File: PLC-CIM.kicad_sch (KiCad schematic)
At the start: 1 part, among them U1 ESP32-DEVKITC

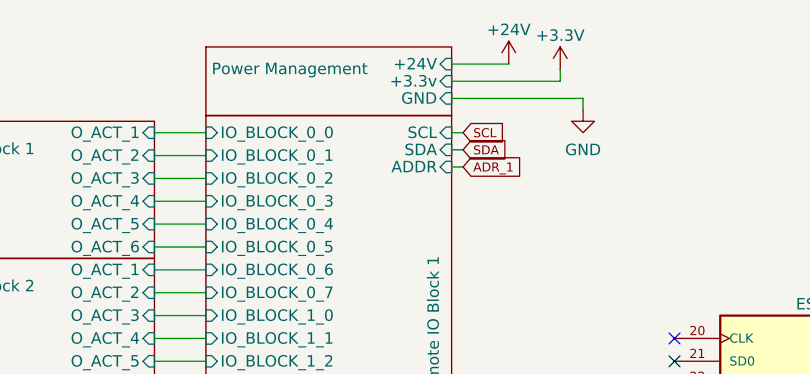
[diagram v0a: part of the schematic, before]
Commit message: Automate library addition * Added script to automagically extract samacsys libraries and put them in corresponding folders. * Note: Requires zsh
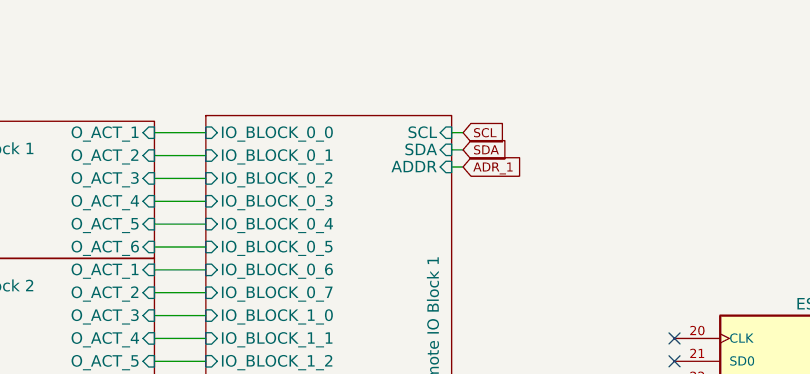
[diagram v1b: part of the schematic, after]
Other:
- removed sheet Power Management
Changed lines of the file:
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@@
-    (stroke (width 0) (type default))
-  )
-  (wire (pts (xy 120.65 63.5) (xy 132.715 63.5))
     (stroke (width 0) (type default))
   )
@@
     (stroke (width 0) (type default))
   )
-  (wire (pts (xy 135.255 65.405) (xy 120.65 65.405))
-    (stroke (width 0) (type default))
-  )
   (wire (pts (xy 120.65 171.45) (xy 122.555 171.45))
     (stroke (width 0) (type default))
@@
     (stroke (width 0) (type default))
   )
-  (wire (pts (xy 135.255 66.675) (xy 135.255 65.405))
-    (stroke (width 0) (type default))
-  )
   (wire (pts (xy 136.525 123.825) (xy 136.525 122.555))
     (stroke (width 0) (type default))
@@
     (stroke (width 0) (type default))
   )
-  (wire (pts (xy 120.65 61.595) (xy 127 61.595))
-    (stroke (width 0) (type default))
-  )
   (wire (pts (xy 90.17 128.905) (xy 93.345 128.905))
     (stroke (width 0) (type default))
@@
     (stroke (width 0) (type default))
   )
-  (wire (pts (xy 132.715 63.5) (xy 132.715 62.23))
-    (stroke (width 0) (type default))
-  )
   (wire (pts (xy 120.65 180.975) (xy 122.555 180.975))
     (stroke (width 0) (type default))
@@
     )
   )
-  (symbol (lib_id "power:GND") (at 135.255 66.675 0) (unit 1)
+  (symbol (lib_id "power:+3.3V") (at 198.12 137.795 0) (unit 1)
     (in_bom yes) (on_board yes) (dnp no) (fields_autoplaced)
-    (property "Reference" "#PWR088" (at 135.255 73.025 0)
-      (effects (font (size 1.27 1.27)) hide)
-    )
-    (property "Value" "GND" (at 135.255 71.12 0)
+    (property "Reference" "#PWR0102" (at 198.12 141.605 0)
+      (effects (font (size 1.27 1.27)) hide)
+    )
+    (property "Value" "+3.3V" (at 198.12 133.985 0)
       (effects (font (size 1.27 1.27)))
     )
-    (property "Footprint" "" (at 135.255 66.675 0)
-      (effects (font (size 1.27 1.27)) hide)
-    )
-    (property "Datasheet" "" (at 135.255 66.675 0)
+    (property "Footprint" "" (at 198.12 137.795 0)
+      (effects (font (size 1.27 1.27)) hide)
+    )
+    (property "Datasheet" "" (at 198.12 137.795 0)
       (effects (font (size 1.27 1.27)) hide)
     )
@@
       (project "PLC-CIM"
         (path "/98f81d77-8880-491b-a7cf-4c27e2d73edf"
-          (reference "#PWR088") (unit 1)
+          (reference "#PWR0102") (unit 1)
         )
       )
     )
   )
-  (symbol (lib_id "power:+3.3V") (at 198.12 137.795 0) (unit 1)
-    (in_bom yes) (on_board yes) (dnp no) (fields_autoplaced)
-    (property "Reference" "#PWR087" (at 198.12 141.605 0)
-      (effects (font (size 1.27 1.27)) hide)
-    )
-    (property "Value" "+3.3V" (at 198.12 133.985 0)
+  (symbol (lib_id "power:GND") (at 198.755 104.775 0) (unit 1)
+    (in_bom yes) (on_board yes) (dnp no)
+    (property "Reference" "#PWR0101" (at 198.755 111.125 0)
+      (effects (font (size 1.27 1.27)) hide)
+    )
+    (property "Value" "GND" (at 202.565 106.045 0)
       (effects (font (size 1.27 1.27)))
     )
-    (property "Footprint" "" (at 198.12 137.795 0)
-      (effects (font (size 1.27 1.27)) hide)
-    )
-    (property "Datasheet" "" (at 198.12 137.795 0)
+    (property "Footprint" "" (at 198.755 104.775 0)
+      (effects (font (size 1.27 1.27)) hide)
+    )
+    (property "Datasheet" "" (at 198.755 104.775 0)
       (effects (font (size 1.27 1.27)) hide)
     )
@@
       (project "PLC-CIM"
         (path "/98f81d77-8880-491b-a7cf-4c27e2d73edf"
-          (reference "#PWR087") (unit 1)
-        )
-      )
-    )
-  )
-  (symbol (lib_id "power:GND") (at 198.755 104.775 0) (unit 1)
-    (in_bom yes) (on_board yes) (dnp no)
-    (property "Reference" "#PWR073" (at 198.755 111.125 0)
-      (effects (font (size 1.27 1.27)) hide)
-    )
-    (property "Value" "GND" (at 202.565 106.045 0)
-      (effects (font (size 1.27 1.27)))
-    )
-    (property "Footprint" "" (at 198.755 104.775 0)
-      (effects (font (size 1.27 1.27)) hide)
-    )
-    (property "Datasheet" "" (at 198.755 104.775 0)
-      (effects (font (size 1.27 1.27)) hide)
-    )
-    (pin "1")
-    (instances
-      (project "PLC-CIM"
-        (path "/98f81d77-8880-491b-a7cf-4c27e2d73edf"
-          (reference "#PWR073") (unit 1)
+          (reference "#PWR0101") (unit 1)
         )
       )
@@
   (symbol (lib_id "power:GND") (at 136.525 139.065 0) (unit 1)
     (in_bom yes) (on_board yes) (dnp no)
-    (property "Reference" "#PWR079" (at 136.525 145.415 0)
+    (property "Reference" "#PWR0106" (at 136.525 145.415 0)
       (effects (font (size 1.27 1.27)) hide)
     )
@@
       (project "PLC-CIM"
         (path "/98f81d77-8880-491b-a7cf-4c27e2d73edf"
-          (reference "#PWR079") (unit 1)
+          (reference "#PWR0106") (unit 1)
         )
       )
@@
   (symbol (lib_id "power:GND") (at 136.525 123.825 0) (unit 1)
     (in_bom yes) (on_board yes) (dnp no)
-    (property "Reference" "#PWR080" (at 136.525 130.175 0)
+    (property "Reference" "#PWR0107" (at 136.525 130.175 0)
       (effects (font (size 1.27 1.27)) hide)
     )
@@
       (project "PLC-CIM"
         (path "/98f81d77-8880-491b-a7cf-4c27e2d73edf"
-          (reference "#PWR080") (unit 1)
-        )
-      )
-    )
-  )
-  (symbol (lib_id "power:+3.3V") (at 132.715 62.23 0) (unit 1)
-    (in_bom yes) (on_board yes) (dnp no) (fields_autoplaced)
-    (property "Reference" "#PWR084" (at 132.715 66.04 0)
-      (effects (font (size 1.27 1.27)) hide)
-    )
-    (property "Value" "+3.3V" (at 132.715 58.42 0)
-      (effects (font (size 1.27 1.27)))
-    )
-    (property "Footprint" "" (at 132.715 62.23 0)
-      (effects (font (size 1.27 1.27)) hide)
-    )
-    (property "Datasheet" "" (at 132.715 62.23 0)
-      (effects (font (size 1.27 1.27)) hide)
-    )
-    (pin "1")
-    (instances
-      (project "PLC-CIM"
-        (path "/98f81d77-8880-491b-a7cf-4c27e2d73edf"
-          (reference "#PWR084") (unit 1)
+          (reference "#PWR0107") (unit 1)
         )
       )
@@
     )
   )
-  (symbol (lib_id "power:+24V") (at 127 61.595 0) (unit 1)
-    (in_bom yes) (on_board yes) (dnp no)
-    (property "Reference" "#PWR086" (at 127 65.405 0)
-      (effects (font (size 1.27 1.27)) hide)
-    )
-    (property "Value" "+24V" (at 127 57.785 0)
-      (effects (font (size 1.27 1.27)))
-    )
-    (property "Footprint" "" (at 127 61.595 0)
-      (effects (font (size 1.27 1.27)) hide)
-    )
-    (property "Datasheet" "" (at 127 61.595 0)
-      (effects (font (size 1.27 1.27)) hide)
-    )
-    (pin "1")
-    (instances
-      (project "PLC-CIM"
-        (path "/98f81d77-8880-491b-a7cf-4c27e2d73edf"
-          (reference "#PWR086") (unit 1)
-        )
-      )
-    )
-  )
   (sheet (at 54.61 128.905) (size 33.02 15.24)
     (stroke (width 0.1524) (type solid))
@@
       )
     )
-  )
-  (sheet (at 93.345 59.69) (size 27.305 7.62)
-    (stroke (width 0.1524) (type solid))
-    (fill (color 0 0 0 0.0000))
-    (property "Sheetname" "Power Management" (at 93.98 62.865 0)
-      (effects (font (size 1.27 1.27)) (justify left bottom))
-    )
-    (property "Sheetfile" "Blocks/PM.kicad_sch" (at 93.345 67.8946 0)
-      (effects (font (size 1.27 1.27)) (justify left top) hide)
-    )
-    (property "Field2" "" (at 93.345 59.69 0)
-      (effects (font (size 1.27 1.27)) hide)
-    )
-    (pin "+24V" input (at 120.65 61.595 0)
-      (effects (font (size 1.27 1.27)) (justify right))
-    )
-    (pin "GND" input (at 120.65 65.405 0)
-      (effects (font (size 1.27 1.27)) (justify right))
-    )
-    (pin "+3.3v" input (at 120.65 63.5 0)
-      (effects (font (size 1.27 1.27)) (justify right))
-    )
-    (instances
-      (project "PLC-CIM"
-        (path "/98f81d77-8880-491b-a7cf-4c27e2d73edf" (page "10"))
-      )
-    )

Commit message: Testing documentation
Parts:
- removed U1: ESP32-DEVKITC, SnapEDA Library:MODULE_ESP32-DEVKITC, symbol ESP32-DEVKITC:ESP32-DEVKITC
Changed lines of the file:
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@@
-    )
-  )
-  (symbol (lib_id "ESP32-DEVKITC:ESP32-DEVKITC") (at 165.735 114.935 180) (unit 1)
-    (in_bom yes) (on_board yes) (dnp no) (fields_autoplaced)
-    (property "Reference" "U1" (at 165.735 85.725 0)
-      (effects (font (size 1.27 1.27)))
-    )
-    (property "Value" "ESP32-DEVKITC" (at 165.735 88.265 0)
-      (effects (font (size 1.27 1.27)))
-    )
-    (property "Footprint" "SnapEDA Library:MODULE_ESP32-DEVKITC" (at 165.735 114.935 0)
-      (effects (font (size 1.27 1.27)) (justify bottom) hide)
-    )
-    (property "Datasheet" "https://docs.espressif.com/projects/esp-idf/en/latest/esp32/hw-reference/esp32/get-started-devkitc.html" (at 165.735 114.935 0)
-      (effects (font (size 1.27 1.27)) hide)
-    )
-    (property "MANUFACTURER" "" (at 165.735 114.935 0)
-      (effects (font (size 1.27 1.27)) (justify bottom) hide)
-    )
-    (property "STANDARD" "Manufacturer Recommendations" (at 165.735 114.935 0)
-      (effects (font (size 1.27 1.27)) (justify bottom) hide)
-    )
-    (property "PARTREV" "N/A" (at 165.735 114.935 0)
-      (effects (font (size 1.27 1.27)) (justify bottom) hide)
-    )
-    (property "Manufacturer_Name" "Espressif" (at 165.735 114.935 0)
-      (effects (font (size 1.27 1.27)) hide)
-    )
-    (property "Manufacturer_Part_Number" "ESP32-DevKitC V4" (at 165.735 114.935 0)
-      (effects (font (size 1.27 1.27)) hide)
-    )
-    (property "Mouser Part Number" "356-ESP32-DEVKITC" (at 165.735 114.935 0)
-      (effects (font (size 1.27 1.27)) hide)
-    )
-    (property "Mouser Price/Stock" "https://eu.mouser.com/ProductDetail/Espressif-Systems/ESP32-DevKitC?qs=chTDxNqvsyn3pn4VyZwnyQ%3D%3D" (at 165.735 114.935 0)
-      (effects (font (size 1.27 1.27)) hide)
-    )
-    (pin "1")
-    (pin "10")
-    (pin "11")
-    (pin "12")
-    (pin "13")
-    (pin "14")
-    (pin "15")
-    (pin "16")
-    (pin "17")
-    (pin "18")
-    (pin "19")
-    (pin "2")
-    (pin "20")
-    (pin "21")
-    (pin "22")
-    (pin "23")
-    (pin "24")
-    (pin "25")
-    (pin "26")
-    (pin "27")
-    (pin "28")
-    (pin "29")
-    (pin "3")
-    (pin "30")
-    (pin "31")
-    (pin "32")
-    (pin "33")
-    (pin "34")
-    (pin "35")
-    (pin "36")
-    (pin "37")
-    (pin "38")
-    (pin "4")
-    (pin "5")
-    (pin "6")
-    (pin "7")
-    (pin "8")
-    (pin "9")
-    (instances
-      (project "PLC-CIM"
-        (path "/98f81d77-8880-491b-a7cf-4c27e2d73edf"
-          (reference "U1") (unit 1)
-        )
-      )
     )
   )
